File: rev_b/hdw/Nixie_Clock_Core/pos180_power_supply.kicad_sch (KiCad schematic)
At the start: 40 parts, among them Q601 IRFL214, U602 LT3757

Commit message: hid all passive refdes on core PCB
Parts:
- C601, C602, C603, C606: Digi-Key PN (none) -> 1276-6767-1-ND
- C607: Digi-Key PN (none) -> 1276-1009-1-ND
- C? (x3): Digi-Key PN (none) -> 1276-1935-1-ND
- C?: Digi-Key PN (none) -> 1276-2970-1-ND
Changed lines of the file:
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@@
       (effects (font (size 1.27 1.27)) (justify right))
     )
-    (property "Digi-Key PN" "" (at 53.975 55.245 0)
+    (property "Digi-Key PN" "1276-6767-1-ND" (at 53.975 55.245 0)
       (effects (font (size 1.524 1.524)) hide)
     )
@@
       (effects (font (size 1.27 1.27)) (justify right))
     )
-    (property "Digi-Key PN" "" (at 38.735 55.245 0)
+    (property "Digi-Key PN" "1276-6767-1-ND" (at 38.735 55.245 0)
       (effects (font (size 1.524 1.524)) hide)
     )
@@
       (effects (font (size 1.27 1.27)) hide)
     )
-    (property "Digi-Key PN" "" (at 52.07 179.07 0)
+    (property "Digi-Key PN" "1276-1935-1-ND" (at 52.07 179.07 0)
       (effects (font (size 1.524 1.524)) hide)
     )
@@
       (effects (font (size 1.27 1.27)) (justify right))
     )
-    (property "Digi-Key PN" "" (at 84.455 55.245 0)
+    (property "Digi-Key PN" "1276-6767-1-ND" (at 84.455 55.245 0)
       (effects (font (size 1.524 1.524)) hide)
     )
@@
       (effects (font (size 1.27 1.27)) (justify left))
     )
-    (property "Digi-Key PN" "" (at -48.26 245.999 0)
+    (property "Digi-Key PN" "1276-2970-1-ND" (at -48.26 245.999 0)
       (effects (font (size 1.27 1.27)) hide)
     )
@@
       (effects (font (size 1.27 1.27)) (justify right))
     )
-    (property "Digi-Key PN" "" (at 69.215 55.245 0)
+    (property "Digi-Key PN" "1276-6767-1-ND" (at 69.215 55.245 0)
       (effects (font (size 1.524 1.524)) hide)
     )
@@
       (effects (font (size 1.27 1.27)) hide)
     )
-    (property "Digi-Key PN" "" (at 127 179.07 0)
+    (property "Digi-Key PN" "1276-1935-1-ND" (at 127 179.07 0)
       (effects (font (size 1.524 1.524)) hide)
     )
@@
       (effects (font (size 1.27 1.27)) hide)
     )
-    (property "Digi-Key PN" "" (at 51.435 100.965 0)
+    (property "Digi-Key PN" "1276-1935-1-ND" (at 51.435 100.965 0)
       (effects (font (size 1.524 1.524)) hide)
     )
@@
       (effects (font (size 1.27 1.27)) (justify right))
     )
-    (property "Digi-Key PN" "" (at 99.695 125.095 0)
+    (property "Digi-Key PN" "1276-1009-1-ND" (at 99.695 125.095 0)
       (effects (font (size 1.524 1.524)) hide)
     )

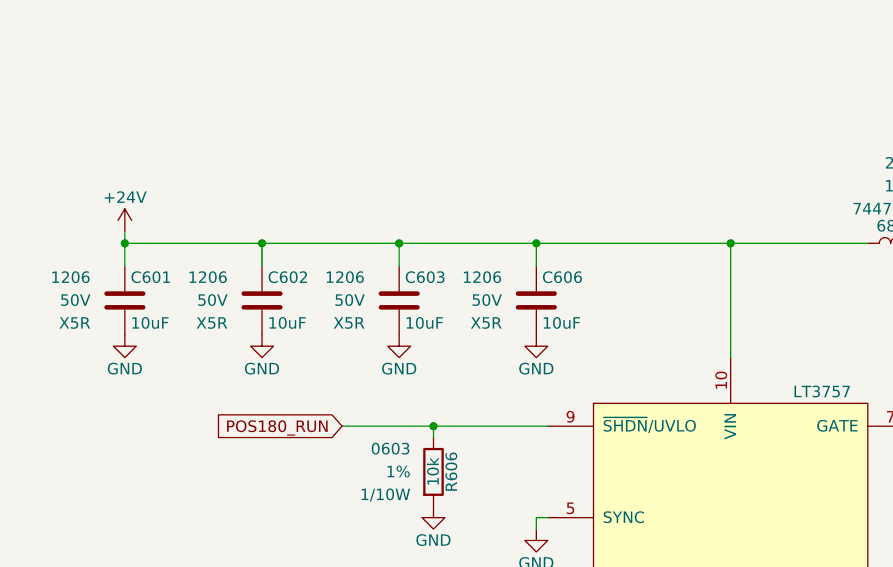
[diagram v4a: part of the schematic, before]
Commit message: more core board component placement
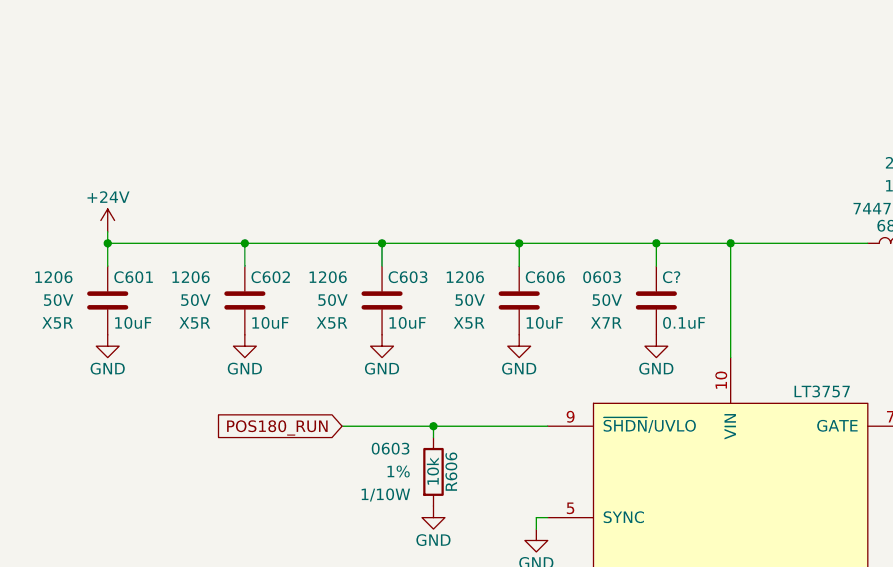
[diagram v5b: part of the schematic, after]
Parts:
- added C?: 0.1uF, Capacitors_SMD:C_0603, symbol Custom_Library:C_Custom
- R610: footprint Resistors_SMD:R_0402 -> Resistors_SMD:R_0603
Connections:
- net +180V: no longer R608.1
- net +24V: now also C?.1
- net +90V: now also R608.1
- net GND: now also C?.2
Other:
- moved on the sheet: C601, C602, C603, C606

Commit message: added BOM
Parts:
- C609, C611, C612: Digi-Key PN (none) -> 399-C1206C104K2RECAUTOCT-ND
- C613: Digi-Key PN (none) -> 565-4697-1-ND
- D601, D602, D603: Digi-Key PN (none) -> SMD1200PL-TPMSCT-ND
- Q601: Footprint Display SOT-223 -> (none); display_footprint (none) -> SOT-223
- R604: Digi-Key PN (none) -> 541-CRCW060314K0FKTACT-ND
- R606, R? (x3): Digi-Key PN (none) -> 541-10.0KHCT-ND
- R608, R613, R?: Digi-Key PN (none) -> 541-1.60MHCT-ND
- R609: Digi-Key PN (none) -> 541-1.33KHCT-ND
- R610: Digi-Key PN (none) -> 541-5537-1-ND
- R614: Digi-Key PN (none) -> 541-28.7KHCT-ND
- R?: Digi-Key PN (none) -> 541-100KHCT-ND
- R?: Digi-Key PN (none) -> 541-3.40KHCT-ND
- R?: Digi-Key PN (none) -> 541-330HCT-ND
- R?: Digi-Key PN (none) -> 541-3951-1-ND
- U602: Digi-Key PN (none) -> LT3757IDD#PBF
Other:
- title: (none) -> Nixie Clock Redux Core Board
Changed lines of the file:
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@@
   (paper "A")
   (title_block
-    (date "2023-05-12")
-    (rev "PRELIM")
+    (title "Nixie Clock Redux Core Board")
+    (date "2023-07-30")
+    (rev "B")
     (company "Drew Maatman")
   )
@@
     (stroke (width 0) (type default))
   )
-  (global_label "POS180_PGOOD" (shape output) (at 66.675 167.64 0)
+  (global_label "POS180_PGOOD" (shape output) (at 66.675 167.64 0) (fields_autoplaced)
     (effects (font (size 1.27 1.27)) (justify left))
-    (property "Intersheetrefs" "${INTERSHEET_REFS}" (at 66.675 167.64 0)
-      (effects (font (size 1.27 1.27)) hide)
+    (property "Intersheetrefs" "${INTERSHEET_REFS}" (at 84.4579 167.64 0)
+      (effects (font (size 1.27 1.27)) (justify left))
     )
   )
-  (global_label "POS180_RUN" (shape input) (at 52.07 81.915 180)
+  (global_label "POS180_RUN" (shape input) (at 52.07 81.915 180) (fields_autoplaced)
     (effects (font (size 1.27 1.27)) (justify right))
-    (property "Intersheetrefs" "${INTERSHEET_REFS}" (at 52.07 81.915 0)
-      (effects (font (size 1.27 1.27)) hide)
+    (property "Intersheetrefs" "${INTERSHEET_REFS}" (at 36.8271 81.915 0)
+      (effects (font (size 1.27 1.27)) (justify right))
     )
   )
-  (global_label "POS180_SNS+" (shape passive) (at 224.79 32.385 90)
+  (global_label "POS180_SNS+" (shape passive) (at 224.79 32.385 90) (fields_autoplaced)
     (effects (font (size 1.27 1.27)) (justify left))
-    (property "Intersheetrefs" "${INTERSHEET_REFS}" (at 224.79 32.385 0)
-      (effects (font (size 1.27 1.27)) hide)
+    (property "Intersheetrefs" "${INTERSHEET_REFS}" (at 224.79 16.8625 90)
+      (effects (font (size 1.27 1.27)) (justify left))
     )
   )
-  (global_label "POS180_SNS-" (shape passive) (at 237.49 32.385 90)
+  (global_label "POS180_SNS-" (shape passive) (at 237.49 32.385 90) (fields_autoplaced)
     (effects (font (size 1.27 1.27)) (justify left))
-    (property "Intersheetrefs" "${INTERSHEET_REFS}" (at 237.49 32.385 0)
-      (effects (font (size 1.27 1.27)) hide)
+    (property "Intersheetrefs" "${INTERSHEET_REFS}" (at 237.49 16.8625 90)
+      (effects (font (size 1.27 1.27)) (justify left))
     )
   )
-  (global_label "POS90_PGOOD" (shape output) (at 141.605 167.64 0)
+  (global_label "POS90_PGOOD" (shape output) (at 141.605 167.64 0) (fields_autoplaced)
     (effects (font (size 1.27 1.27)) (justify left))
-    (property "Intersheetrefs" "${INTERSHEET_REFS}" (at 141.605 167.64 0)
-      (effects (font (size 1.27 1.27)) hide)
+    (property "Intersheetrefs" "${INTERSHEET_REFS}" (at 158.1784 167.64 0)
+      (effects (font (size 1.27 1.27)) (justify left))
     )
   )
@@
       (effects (font (size 1.524 1.524)) hide)
     )
+    (property "Digi-Key PN" "LT3757IDD#PBF" (at 95.25 95.885 0)
+      (effects (font (size 1.27 1.27)) hide)
+    )
     (pin "1")
     (pin "10")
@@
       (effects (font (size 1.27 1.27)) (justify right))
     )
+    (property "Digi-Key PN" "541-10.0KHCT-ND" (at 62.23 86.995 0)
+      (effects (font (size 1.27 1.27)) hide)
+    )
     (pin "1")
     (pin "2")
@@
       (effects (font (size 1.27 1.27)) (justify left))
     )
-    (property "Digi-Key PN" "" (at 88.9 130.175 0)
+    (property "Digi-Key PN" "541-100KHCT-ND" (at 88.9 130.175 0)
       (effects (font (size 1.27 1.27)) hide)
     )
@@
       (effects (font (size 1.27 1.27)) (justify left))
     )
-    (property "Digi-Key PN" "" (at 68.58 148.59 0)
+    (property "Digi-Key PN" "541-10.0KHCT-ND" (at 68.58 148.59 0)
       (effects (font (size 1.524 1.524)) hide)
     )
@@
       (effects (font (size 1.27 1.27)) (justify right))
     )
-    (property "Digi-Key PN" "" (at 208.915 56.515 0)
+    (property "Digi-Key PN" "399-C1206C104K2RECAUTOCT-ND" (at 208.915 56.515 0)
       (effects (font (size 1.524 1.524)) hide)
     )
@@
       (effects (font (size 1.27 1.27)) (justify right))
     )
+    (property "Digi-Key PN" "541-1.60MHCT-ND" (at 162.56 108.585 0)
+      (effects (font (size 1.27 1.27)) hide)
+    )
     (pin "1")
     (pin "2")
@@
       (effects (font (size 1.27 1.27)) (justify right))
     )
+    (property "Digi-Key PN" "541-1.33KHCT-ND" (at 94.615 173.99 0)
+      (effects (font (size 1.27 1.27)) hide)
+    )
     (pin "1")
     (pin "2")
@@
       (effects (font (size 1.27 1.27)) (justify right))
     )
+    (property "Digi-Key PN" "541-5537-1-ND" (at 94.615 186.055 0)
+      (effects (font (size 1.27 1.27)) hide)
+    )
     (pin "1")
     (pin "2")
@@
       (effects (font (size 1.27 1.27)) (justify left))
     )
-    (property "Digi-Key PN" "" (at 27.305 149.86 0)
+    (property "Digi-Key PN" "541-1.60MHCT-ND" (at 27.305 149.86 0)
       (effects (font (size 1.524 1.524)) hide)
     )
@@
       (effects (font (size 1.27 1.27)) (justify left))
     )
-    (property "Digi-Key PN" "" (at 27.305 175.895 0)
+    (property "Digi-Key PN" "541-3.40KHCT-ND" (at 27.305 175.895 0)
       (effects (font (size 1.524 1.524)) hide)
     )
@@
       (effects (font (size 1.27 1.27)) (justify right))
     )
-    (property "Digi-Key PN" "" (at 225.425 40.005 0)
+    (property "Digi-Key PN" "565-4697-1-ND" (at 225.425 40.005 0)
       (effects (font (size 1.524 1.524)) hide)
     )
@@
       (effects (font (size 1.27 1.27)) (justify left))
     )
-    (property "Digi-Key PN" "" (at 143.51 148.59 0)
+    (property "Digi-Key PN" "541-10.0KHCT-ND" (at 143.51 148.59 0)
       (effects (font (size 1.524 1.524)) hide)
     )
@@
       (effects (font (size 1.27 1.27)) (justify left))
     )
-    (property "Digi-Key PN" "" (at 27.305 163.83 0)
+    (property "Digi-Key PN" "541-330HCT-ND" (at 27.305 163.83 0)
       (effects (font (size 1.524 1.524)) hide)
     )
@@
       (effects (font (size 1.27 1.27)) (justify right))
     )
+    (property "Digi-Key PN" "541-1.60MHCT-ND" (at 94.615 160.02 0)
+      (effects (font (size 1.27 1.27)) hide)
+    )
     (pin "1")
     (pin "2")
@@
       (effects (font (size 1.27 1.27)) (justify right))
     )
-    (property "Digi-Key PN" "" (at 145.415 40.005 0)
+    (property "Digi-Key PN" "399-C1206C104K2RECAUTOCT-ND" (at 145.415 40.005 0)
       (effects (font (size 1.524 1.524)) hide)
     )
@@
       (effects (font (size 1.27 1.27)) (justify right))
     )
+    (property "Digi-Key PN" "541-CRCW060314K0FKTACT-ND" (at 48.26 113.665 0)
+      (effects (font (size 1.27 1.27)) hide)
+    )
     (pin "1")
     (pin "2")
@@
       (effects (font (size 1.27 1.27)))
     )
-    (property "Footprint Display" "SOT-223" (at 141.478 85.471 0)
+    (property "Footprint Display" "" (at 141.478 85.471 0)
       (effects (font (size 1.27 1.27)) hide)
     )
@@
       (effects (font (size 1.27 1.27)) hide)
     )
+    (property "display_footprint" "SOT-223" (at 132.08 81.915 0)
+      (effects (font (size 1.27 1.27)) hide)
+    )
     (pin "1")
     (pin "2")
@@
       (effects (font (size 1.27 1.27)) (justify right))
     )
+    (property "Digi-Key PN" "541-28.7KHCT-ND" (at 162.56 126.365 0)
+      (effects (font (size 1.27 1.27)) hide)
+    )
     (pin "1")
     (pin "2")
@@
       (effects (font (size 1.27 1.27)) hide)
     )
-    (property "Digi-Key PN" "" (at 224.79 36.195 0)
+    (property "Digi-Key PN" "541-3951-1-ND" (at 224.79 36.195 0)
       (effects (font (size 1.27 1.27)) hide)
     )
@@
       (effects (font (size 1.27 1.27)) hide)
     )
+    (property "Digi-Key PN" "SMD1200PL-TPMSCT-ND" (at 175.26 45.085 0)
+      (effects (font (size 1.27 1.27)) hide)
+    )
     (pin "1")
     (pin "2")
@@
       (effects (font (size 1.27 1.27)) hide)
     )
+    (property "Digi-Key PN" "SMD1200PL-TPMSCT-ND" (at 149.86 61.595 0)
+      (effects (font (size 1.27 1.27)) hide)
+    )
     (pin "1")
     (pin "2")
@@
       (effects (font (size 1.27 1.27)) (justify right))
     )
-    (property "Digi-Key PN" "" (at 208.915 40.005 0)
+    (property "Digi-Key PN" "399-C1206C104K2RECAUTOCT-ND" (at 208.915 40.005 0)
       (effects (font (size 1.524 1.524)) hide)
     )
@@
       (effects (font (size 1.27 1.27)) hide)
     )
-    (property "Digi-Key PN" "" (at 237.49 36.195 0)
+    (property "Digi-Key PN" "541-10.0KHCT-ND" (at 237.49 36.195 0)
       (effects (font (size 1.27 1.27)) hide)
     )
@@
       (effects (font (size 1.27 1.27)) hide)
     )
+    (property "Digi-Key PN" "SMD1200PL-TPMSCT-ND" (at 162.56 52.705 0)
+      (effects (font (size 1.27 1.27)) hide)
+    )
